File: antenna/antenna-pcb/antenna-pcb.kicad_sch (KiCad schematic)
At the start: 11 parts, among them J1 SMA Connector Male, U1 HHM1589D1

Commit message: bottom adapter plate sanity commit
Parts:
- added Burn1, Burn2, Burn3, Burn4: Burn, TestPoint:TestPoint_THTPad_2.0x2.0mm_Drill1.0mm, symbol Connector:TestPoint
- added GND1, GND2, GND3, GND4: GND, TestPoint:TestPoint_THTPad_2.0x2.0mm_Drill1.0mm, symbol Connector:TestPoint
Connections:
- net GND: now also GND1.1, GND2.1, GND3.1, GND4.1
- new net BURN: Burn1.1, Burn2.1, Burn3.1, Burn4.1
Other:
- moved on the sheet: AE1, J1, U1

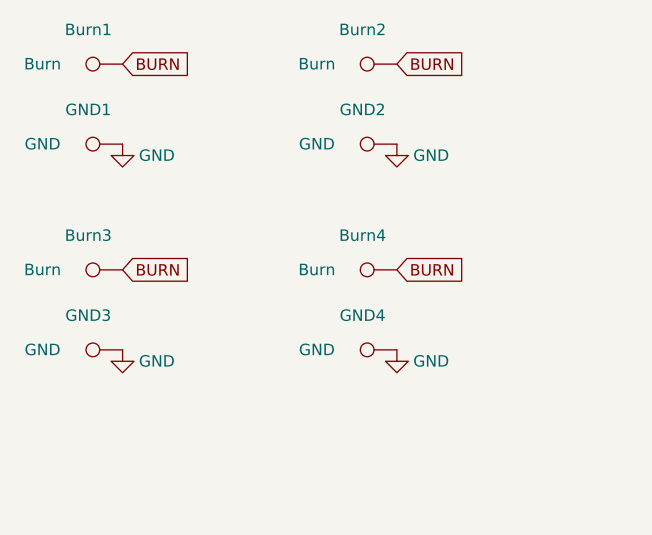
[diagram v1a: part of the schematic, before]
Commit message: placed components, added traces to antenna-solar
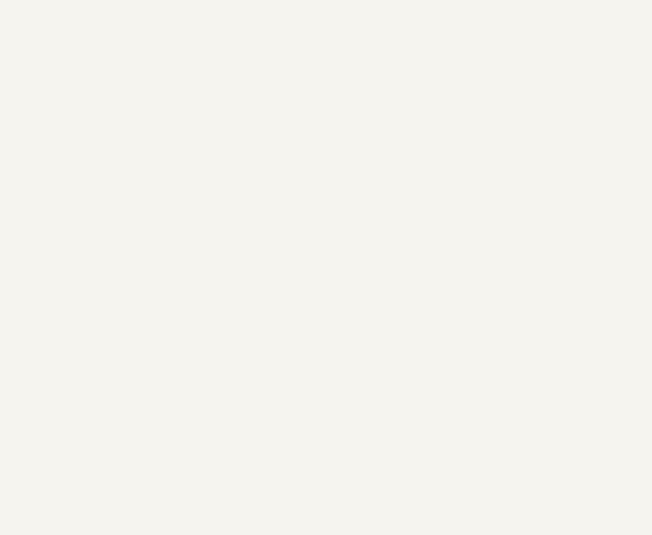
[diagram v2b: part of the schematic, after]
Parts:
- removed Burn1, Burn2, Burn3, Burn4: Burn, TestPoint:TestPoint_THTPad_2.0x2.0mm_Drill1.0mm, symbol Connector:TestPoint
- removed GND1, GND2, GND3, GND4: GND, TestPoint:TestPoint_THTPad_2.0x2.0mm_Drill1.0mm, symbol Connector:TestPoint

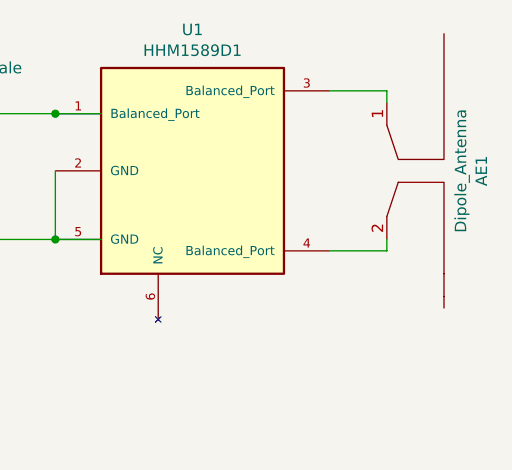
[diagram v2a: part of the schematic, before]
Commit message: fixed balun placement and wiring
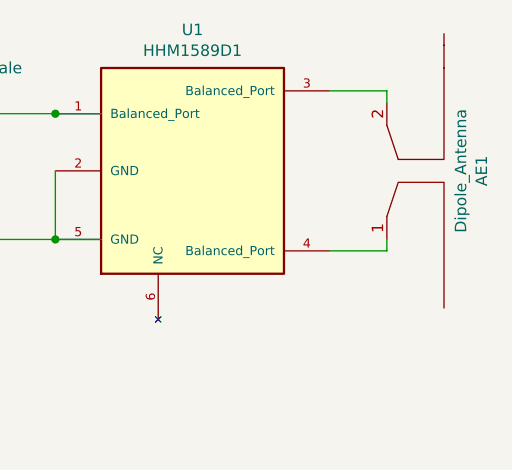
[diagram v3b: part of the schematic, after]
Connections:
- net at AE1.1: now also U1.4 (Balanced_Port); no longer U1.3 (Balanced_Port)
- net at AE1.2: now also U1.3 (Balanced_Port); no longer U1.4 (Balanced_Port)
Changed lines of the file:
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@@
     (pin "2")
   )
-  (symbol (lib_id "solar-panel-side-Z-minus-rescue:UHF_Dipole_Antenna-sapling") (at 226.06 62.23 270) (unit 1)
+  (symbol (lib_id "solar-panel-side-Z-minus-rescue:UHF_Dipole_Antenna-sapling") (at 226.06 62.23 270) (mirror x) (unit 1)
     (in_bom yes) (on_board yes)
     (property "Reference" "AE1" (id 0) (at 231.521 62.23 0))
